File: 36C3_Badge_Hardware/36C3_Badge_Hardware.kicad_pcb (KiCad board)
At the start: 2 copper layers, 160 x 100 mm, 0 parts

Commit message: First revision of PCB
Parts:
- added BT1: 1S LiIon, custom:1S_18650_Holder_with_Spacers, B.Cu at (89.1, 116.8)
- added C1: 10µ/25V, Capacitors_SMD:C_0805, B.Cu at (124.3, 121.0)
- added C10: 470n/50V, Capacitors_SMD:C_0805, B.Cu at (175.2, 52.5)
- added C11: 470n/50V, Capacitors_SMD:C_0805, B.Cu at (172.6, 52.5)
- added C12: 470n/50V, Capacitors_SMD:C_0805, B.Cu at (170.0, 52.5)
- added C13: 470n/50V, Capacitors_SMD:C_0805, B.Cu at (167.4, 52.5)
- added C14: 470n/50V, Capacitors_SMD:C_0805, B.Cu at (164.8, 52.5)
- added C15: 470n/50V, Capacitors_SMD:C_0805, B.Cu at (162.2, 52.5)
- added C16: 470n/50V, Capacitors_SMD:C_0805, B.Cu at (159.6, 52.5)
- added C17: 470n/50V, Capacitors_SMD:C_0805, B.Cu at (157.0, 52.5)
- added C18: 100n, Capacitors_SMD:C_0603, B.Cu at (100.0, 80.4)
- added C19: 100n, Capacitors_SMD:C_0603, B.Cu at (100.0, 78.8)
- added C2: 4.7µ/25V, Capacitors_SMD:C_0805, B.Cu at (117.8, 115.3)
- added C20: 100n, Capacitors_SMD:C_0603, B.Cu at (120.0, 78.0)
- added C21: 100n, Capacitors_SMD:C_0603, B.Cu at (79.7, 43.8)
- added C22: 100n, Capacitors_SMD:C_0603, B.Cu at (70.7, 43.8)
- added C23: 82p, Capacitors_SMD:C_0603, B.Cu at (142.0, 64.5)
- added C24: 100n, Capacitors_SMD:C_0603, B.Cu at (61.7, 43.8)
- added C25: 100n, Capacitors_SMD:C_0603, B.Cu at (52.7, 43.8)
- added C26: 18p, Capacitors_SMD:C_0603, B.Cu at (100.0, 77.2)
- added C27: 100n, Capacitors_SMD:C_0603, B.Cu at (111.3, 90.0)
- added C28: 18p, Capacitors_SMD:C_0603, B.Cu at (91.8, 77.2)
- added C3: 100n, Capacitors_SMD:C_0603, B.Cu at (81.6, 111.9)
- added C4: 100n, Capacitors_SMD:C_0603, B.Cu at (171.2, 117.7)
- added C5: 100n, Capacitors_SMD:C_0603, B.Cu at (176.6, 114.8)
- added C6: 22µ/25V, Capacitors_SMD:C_0805, B.Cu at (121.2, 106.0)
- added C7: 4.7µ/25V, Capacitors_SMD:C_0805, B.Cu at (126.6, 121.0)
- added C8: 4.7µ/25V, Capacitors_SMD:C_0805, B.Cu at (117.8, 122.6)
- added C9: 100n, Capacitors_SMD:C_0603, B.Cu at (179.7, 56.3)
- added D1: USBLC6-2SC6, TO_SOT_Packages_SMD:SOT-23-6, B.Cu at (181.5, 115.4)
- added D10: Destruction3, custom:LED_SideFacing_0802, B.Cu at (133.9, 55.5)
- added D11: Destruction3, custom:LED_SideFacing_0802, B.Cu at (139.3, 47.9)
- added D12: Destruction3, custom:LED_SideFacing_0802, B.Cu at (143.5, 37.8)
- added D13: Destruction3, custom:LED_SideFacing_0802, B.Cu at (150.7, 31.9)
- added D14: Destruction2, custom:LED_SideFacing_0802, B.Cu at (32.0, 54.5)
- added D15: Destruction2, custom:LED_SideFacing_0802, B.Cu at (36.4, 55.9)
- added D16: Destruction2, custom:LED_SideFacing_0802, B.Cu at (41.6, 56.8)
- added D17: Destruction2, custom:LED_SideFacing_0802, B.Cu at (50.2, 59.3)
- added D18: Destruction2, custom:LED_SideFacing_0802, B.Cu at (60.6, 64.2)
- added D19: Destruction2, custom:LED_SideFacing_0802, B.Cu at (71.0, 66.2)
- added D2: SK110, Diodes_SMD:D_SMA_Standard, B.Cu at (118.0, 106.3)
- added D20: Destruction2, custom:LED_SideFacing_0802, B.Cu at (66.3, 61.7)
- added D21: Destruction2, custom:LED_SideFacing_0802, B.Cu at (57.5, 57.1)
- added D22: Destruction2, custom:LED_SideFacing_0802, B.Cu at (46.3, 50.2)
- added D23: Destruction2, custom:LED_SideFacing_0802, B.Cu at (39.7, 46.9)
- added D24: Destruction2, custom:LED_SideFacing_0802, B.Cu at (32.6, 42.6)
- added D25: Destruction1, custom:LED_SideFacing_0802, B.Cu at (31.8, 116.4)
- added D26: Destruction1, custom:LED_SideFacing_0802, B.Cu at (37.3, 114.5)
- added D27: Destruction1, custom:LED_SideFacing_0802, B.Cu at (45.3, 111.5)
- added D28: Destruction1, custom:LED_SideFacing_0802, B.Cu at (54.7, 104.4)
- added D29: Destruction1, custom:LED_SideFacing_0802, B.Cu at (47.1, 103.8)
- added D3: USB, LEDs:LED_0603, B.Cu at (167.4, 126.3)
- added D30: Destruction1, custom:LED_SideFacing_0802, B.Cu at (40.3, 107.9)
- added D31: Destruction1, custom:LED_SideFacing_0802, B.Cu at (31.8, 106.8)
- added D32: BAT54S, TO_SOT_Packages_SMD:SOT-23, B.Cu at (175.2, 48.2)
- added D33: BAT54S, TO_SOT_Packages_SMD:SOT-23, B.Cu at (170.0, 48.2)
- added D34: Hope2, custom:LED_SideFacing_0802, B.Cu at (188.2, 95.2)
- added D35: Hope2, custom:LED_SideFacing_0802, B.Cu at (181.7, 96.7)
- added D36: Hope2, custom:LED_SideFacing_0802, B.Cu at (176.5, 98.0)
- added D37: Hope2, custom:LED_SideFacing_0802, B.Cu at (166.8, 101.7)
- added D38: Hope2, custom:LED_SideFacing_0802, B.Cu at (158.2, 105.1)
- added D39: Hope2, custom:LED_SideFacing_0802, B.Cu at (150.1, 108.2)
- added D4: Rx, LEDs:LED_0603, B.Cu at (167.4, 122.7)
- added D40: Hope2, custom:LED_SideFacing_0802, B.Cu at (137.9, 111.8)
- added D41: Hope2, custom:LED_SideFacing_0802, B.Cu at (127.7, 114.7)
- added D42: Hope2, custom:LED_SideFacing_0802, B.Cu at (132.5, 117.2)
- added D43: Hope2, custom:LED_SideFacing_0802, B.Cu at (144.6, 114.7)
- added D44: Hope2, custom:LED_SideFacing_0802, B.Cu at (153.7, 114.3)
- added D45: Hope2, custom:LED_SideFacing_0802, B.Cu at (164.4, 111.1)
- added D46: Hope2, custom:LED_SideFacing_0802, B.Cu at (172.3, 108.6)
- added D47: Hope2, custom:LED_SideFacing_0802, B.Cu at (181.8, 106.3)
- added D48: Hope2, custom:LED_SideFacing_0802, B.Cu at (188.1, 107.6)
- added D49: BAT54S, TO_SOT_Packages_SMD:SOT-23, B.Cu at (164.8, 48.2)
- added D5: Tx, LEDs:LED_0603, B.Cu at (167.4, 119.1)
- added D50: Hope1, custom:LED_SideFacing_0802, B.Cu at (88.5, 31.9)
- added D51: Hope1, custom:LED_SideFacing_0802, B.Cu at (90.4, 41.5)
- added D52: Hope1, custom:LED_SideFacing_0802, B.Cu at (92.5, 51.6)
- added D53: Hope1, custom:LED_SideFacing_0802, B.Cu at (96.6, 46.7)
- added D54: Hope1, custom:LED_SideFacing_0802, B.Cu at (96.3, 37.1)
- added D55: Hope1, custom:LED_SideFacing_0802, B.Cu at (95.7, 31.8)
- added D56: BAT46W, Diodes_SMD:D_SOD-123, B.Cu at (159.5, 48.8)
- added D57: 1N4148, Diodes_SMD:D_0603, B.Cu at (162.4, 61.6)
- added D58: 1N4148, Diodes_SMD:D_0603, B.Cu at (159.7, 59.9)
- added D59: 1N4148, Diodes_SMD:D_0603, B.Cu at (159.7, 63.3)
- added D7: Destruction3, custom:LED_SideFacing_0802, B.Cu at (140.7, 32.1)
- added D8: Destruction3, custom:LED_SideFacing_0802, B.Cu at (136.2, 41.5)
- added D9: Destruction3, custom:LED_SideFacing_0802, B.Cu at (132.3, 48.4)
- added G***: resource_exhaustion_mask, custom:resource_exhaustion_mask, F.Cu at (84.1, 103.3)
- added J1: MicroUSB, custom:MicroUSB_Amphenol_10118192, B.Cu at (188.5, 115.4)
- added J2: ISP, Pin_Headers:Pin_Header_Straight_SMT_02x03, B.Cu at (135.0, 80.0)
- added JP1: ISP, custom:Jumper_SolderBridge, B.Cu at (157.5, 63.3)
- added L1: 4.7µ/1.25A, custom:Inductor_3x3mm, B.Cu at (117.2, 111.7)
- added Q1: FS8205A, Housings_SSOP:TSSOP-8_4.4x3mm_Pitch0.65mm, B.Cu at (91.6, 114.0)
- added Q10: MMBTA42, TO_SOT_Packages_SMD:SOT-23, B.Cu at (98.4, 42.4)
- added Q2: MMBTA42, TO_SOT_Packages_SMD:SOT-23, B.Cu at (139.0, 52.7)
- added Q3: MMBTA42, TO_SOT_Packages_SMD:SOT-23, B.Cu at (47.8, 61.3)
- added Q4: MMBTA92, TO_SOT_Packages_SMD:SOT-23, B.Cu at (171.4, 58.2)
- added Q5: MMBTA42, TO_SOT_Packages_SMD:SOT-23, B.Cu at (171.4, 63.2)
- added Q6: MMBTA42, TO_SOT_Packages_SMD:SOT-23, B.Cu at (35.1, 117.5)
- added Q7: MMBTA42, TO_SOT_Packages_SMD:SOT-23, B.Cu at (160.5, 100.1)
- added Q8: MMBTA92, TO_SOT_Packages_SMD:SOT-23, B.Cu at (166.0, 58.2)
- added Q9: MMBTA42, TO_SOT_Packages_SMD:SOT-23, B.Cu at (166.0, 63.2)
- added R1: 100R, Resistors_SMD:R_0603, B.Cu at (78.9, 111.9)
- added R10: 1k, Resistors_SMD:R_0603, B.Cu at (164.1, 126.3)
- added R11: 1k, Resistors_SMD:R_0603, B.Cu at (164.1, 122.7)
- added R12: 1k, Resistors_SMD:R_0603, B.Cu at (164.1, 119.1)
- added R14: 1k, Resistors_SMD:R_Array_Concave_4x0603, B.Cu at (127.4, 41.2)
- added R15: 1k, Resistors_SMD:R_Array_Concave_4x0603, B.Cu at (149.5, 42.3)
- added R16: 4.7k, Resistors_SMD:R_0603, B.Cu at (140.0, 56.5)
- added R17: 1k, Resistors_SMD:R_Array_Concave_4x0603, B.Cu at (39.1, 60.5)
- added R18: 1k, Resistors_SMD:R_Array_Concave_4x0603, B.Cu at (73.0, 59.0)
- added R19: 1k, Resistors_SMD:R_Array_Concave_4x0603, B.Cu at (42.3, 42.1)
- added R2: 2k, Resistors_SMD:R_0603, B.Cu at (117.8, 125.0)
- added R20: 4.7k, Resistors_SMD:R_0603, B.Cu at (48.8, 65.0)
- added R21: 1k, Resistors_SMD:R_0603, B.Cu at (175.0, 57.3)
- added R22: 1k, Resistors_SMD:R_0603, B.Cu at (175.0, 64.1)
- added R23: 1k, Resistors_SMD:R_Array_Concave_4x0603, B.Cu at (41.9, 118.7)
- added R24: 1k, Resistors_SMD:R_Array_Concave_4x0603, B.Cu at (39.3, 102.1)
- added R25: 4.7k, Resistors_SMD:R_0603, B.Cu at (36.1, 121.2)
- added R26: 1k, Resistors_SMD:R_Array_Concave_4x0603, B.Cu at (178.5, 92.0)
- added R27: 1k, Resistors_SMD:R_Array_Concave_4x0603, B.Cu at (143.6, 103.9)
- added R28: 1k, Resistors_SMD:R_Array_Concave_4x0603, B.Cu at (149.2, 120.8)
- added R29: 1k, Resistors_SMD:R_Array_Concave_4x0603, B.Cu at (176.3, 111.1)
- added R3: 1k, Resistors_SMD:R_0603, B.Cu at (88.2, 110.7)
- added R30: 4.7k, Resistors_SMD:R_0603, B.Cu at (156.7, 101.1)
- added R31: 1k, Resistors_SMD:R_0603, B.Cu at (162.4, 59.1)
- added R32: 1k, Resistors_SMD:R_0603, B.Cu at (162.4, 64.1)
- added R33: 1k, Resistors_SMD:R_Array_Concave_4x0603, B.Cu at (87.1, 47.2)
- added R34: 1k, Resistors_SMD:R_Array_Concave_4x0603, B.Cu at (101.1, 35.1)
- added R35: 470R, Resistors_SMD:R_0603, B.Cu at (155.1, 48.8)
- added R36: 4.7k, Resistors_SMD:R_0603, B.Cu at (102.1, 41.4)
- added R37: 1k, Resistors_SMD:R_0603, B.Cu at (82.8, 43.8)
- added R38: 1k, Resistors_SMD:R_0603, B.Cu at (73.8, 43.8)
- added R39: 8.2k, Resistors_SMD:R_0603, B.Cu at (144.1, 64.5)
- added R4: 330k, Resistors_SMD:R_0603, B.Cu at (129.7, 122.9)
- added R40: 1k, Resistors_SMD:R_0603, B.Cu at (64.8, 43.8)
- added R41: 1k, Resistors_SMD:R_0603, B.Cu at (55.8, 43.8)
- added R42: 100k, Resistors_SMD:R_0603, B.Cu at (120.0, 82.0)
- added R43: 10k, Resistors_SMD:R_0603, B.Cu at (109.6, 90.0)
- added R5: 120k, Resistors_SMD:R_0603, B.Cu at (129.7, 125.1)
- added R6: 18k, Resistors_SMD:R_0603, B.Cu at (117.8, 127.1)
- added R7: 10k, Resistors_SMD:R_0603, B.Cu at (129.7, 127.3)
- added R8: 5.6k, Resistors_SMD:R_0603, B.Cu at (123.5, 106.0)
- added R9: 1.82k, Resistors_SMD:R_0603, B.Cu at (123.5, 109.3)
- added REF**: MountingHole_3mm, Mounting_Holes:MountingHole_3mm, F.Cu at (179.1, 37.5)
- added REF**: StandBy_H3.5mm, custom:StandBy_H3.5mm, B.Cu at (54.2, 49.6)
- added REF**: MountingHole_3mm, Mounting_Holes:MountingHole_3mm, F.Cu at (37.5, 37.5)
- added SW1: Reset, Buttons_Switches_SMD:SW_SPST_SKQG, B.Cu at (81.2, 38.3)
- added SW2: Button1, Buttons_Switches_SMD:SW_SPST_SKQG, B.Cu at (72.2, 38.3)
- added SW3: Button2, Buttons_Switches_SMD:SW_SPST_SKQG, B.Cu at (63.2, 38.3)
- added SW4: Standby, Buttons_Switches_SMD:SW_SPST_SKQG, B.Cu at (54.2, 38.3)
- added U1: MIC2288, TO_SOT_Packages_SMD:SOT-23-5, B.Cu at (121.0, 114.1)
- added U2: DW01, TO_SOT_Packages_SMD:SOT-23-6, B.Cu at (85.0, 111.9)
- added U3: MCP73871-2CCI, Housings_DFN_QFN:QFN-20-1EP_4x4mm_Pitch0.5mm, B.Cu at (123.9, 125.8)
- added U4: CH330N, Housings_SOIC:SOIC-8_3.9x4.9mm_Pitch1.27mm, B.Cu at (175.5, 119.7)
- added U5: 74LVC2G17, custom:SOT-457, B.Cu at (178.9, 53.5)
- added U6: ATMEGA328P-AU, Housings_QFP:TQFP-32_7x7mm_Pitch0.8mm, B.Cu at (110.0, 80.0)
- added VFD1: HCS-12SS59T, custom:VFD_HCS-12SS59T_noSilk, F.Cu at (110.0, 80.0)
- added Y1: 16MHz, Crystals:Crystal_HC49-SD_SMD, B.Cu at (95.9, 73.5)
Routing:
- net +5V: track 0.00 -> 850.7 mm, vias 0 -> 3
- net Net-(D34-Pad1): track 0.00 -> 160.0 mm, vias 0 -> 16
- net /FIL+: track 0.00 -> 139.8 mm, vias 0 -> 3
- net /UART_RX: track 0.00 -> 132.0 mm, vias 0 -> 2
- net /UART_TX: track 0.00 -> 131.8 mm, vias 0 -> 2
- net Net-(D14-Pad1): track 0.00 -> 113.6 mm, vias 0 -> 11
- net /UART_RTS: track 0.00 -> 111.7 mm, vias 0 -> 2
- net /SW_RESET: track 0.00 -> 110.8 mm, vias 0 -> 4
- net /PMIC_~PG: track 0.00 -> 110.6 mm, vias 0 -> 4
- net /LED_D1: track 0.00 -> 108.2 mm, vias 0 -> 2
- net +BATT: track 0.00 -> 95.5 mm
- net +5V_USB: track 0.00 -> 92.7 mm
- net /VFD_SUP_CLK_A: track 0.00 -> 91.6 mm, vias 0 -> 4
- net /VFD_SUP_CLK_B: track 0.00 -> 90.9 mm, vias 0 -> 4
- net Net-(D10-Pad1): track 0.00 -> 85.4 mm, vias 0 -> 8
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- added copper zone on B.Cu, net +5V
- added copper zone on B.Cu, net +5V_USB
- added copper zone on B.Cu, net +BATT
- added copper zone on B.Cu, net -BATT
- added copper zone on B.Cu, net GND
- added copper zone on F.Cu, net GND
- added copper zone on B.Cu, net Net-(D2-Pad2)
- added copper zone on B.Cu, net VCC
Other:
- rule via_min_drill: 0.3 -> 0.2
- board text added: "A"
- board text added: "B"
- board text added: "Designed by Cato - @Mezgrman Rev. 1.0 / 08.12.2019"
- board text added: "I"
- board text added: "O"
- board text added: "Reset"
- board text added: "USB"

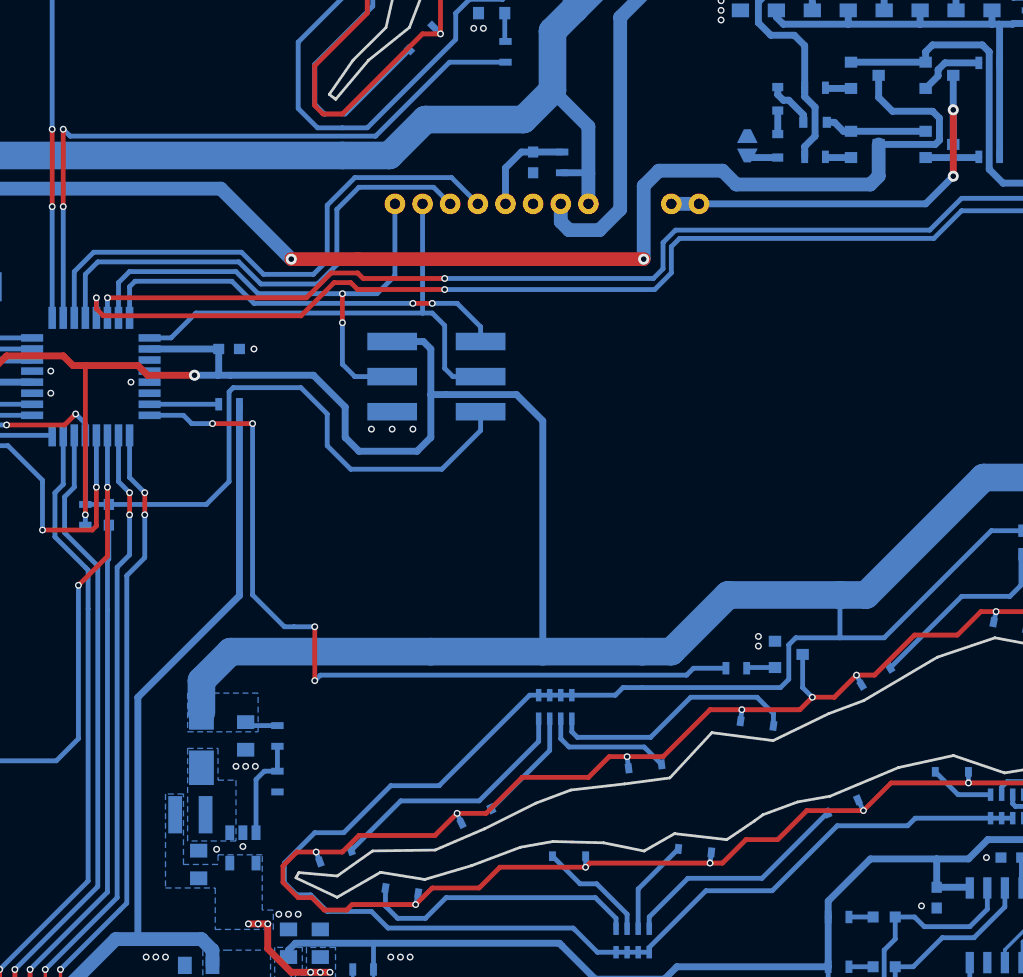
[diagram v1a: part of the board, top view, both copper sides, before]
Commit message: Schematic / Board updates and bugfixes:
- Updated crack LED resistor values after testing
- Changed microcontroller reset capacitor from 100nF to 1µF and case from 0603 to 0805
- Changed MMBTA type transistors to BC types (MMBTA didn't work in the VFD filament H-Bridge)
- Added Schottky diode in series to CH330 VCC pin. This fixes an error where the badge would erroneously detect USB power when the CH330 was backfed via the high Tx pin.
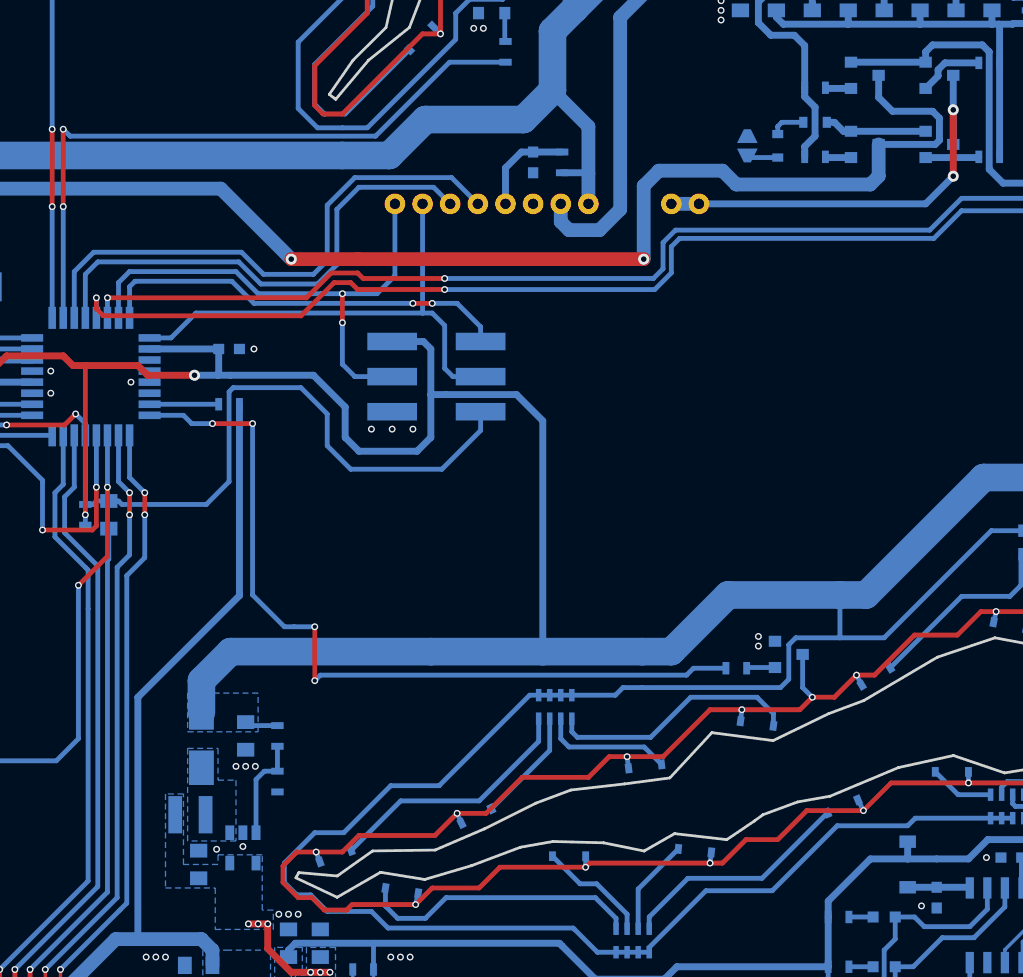
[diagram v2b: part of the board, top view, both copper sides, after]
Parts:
- removed D59: 1N4148, Diodes_SMD:D_0603
- added D6: BAT46W, Diodes_SMD:D_SOD-123, B.Cu at (169.1, 115.3)
- C27: value 100n -> 1µ; footprint Capacitors_SMD:C_0603 -> Capacitors_SMD:C_0805
- Q10, Q2, Q3, Q5, Q6, Q7, Q9: value MMBTA42 -> BC817
- Q4, Q8: value MMBTA92 -> BC807
- R14, R15, R17, R18, R19, R23, R24: value 1k -> 470R
- R26, R27, R28, R29, R33, R34: value 1k -> 2.2k
- moved D58 3.40 mm to (159.7, 63.3)
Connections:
- C4 pad 2: +5V_USB -> Net-(C4-Pad2)
- JP1 pad 1: Net-(D59-Pad1) -> Net-(D58-Pad1)
- U4 pad 5: +5V_USB -> Net-(C4-Pad2)
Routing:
- net Net-(C4-Pad2): track 0.00 -> 4.52 mm
- net +5V_USB: track 92.7 -> 89.5 mm
- net Net-(D59-Pad1): track 2.26 -> 0.00 mm
- net Net-(D57-Pad1): track 3.55 -> 2.52 mm
- net Net-(D58-Pad1): track 1.70 -> 2.26 mm
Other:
- board text added: "Designed by Cato - @Mezgrman Rev. 1.1 / 22.12.2019"
- board text removed: "Designed by Cato - @Mezgrman Rev. 1.0 / 08.12.2019"
